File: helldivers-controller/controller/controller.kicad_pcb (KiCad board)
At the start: 4 copper layers, 71 x 57 mm, 9 parts, among them SW10 SW_Push, SW11 SW_Push, SW2 SW_SPDT, SW3 SW_SPDT, SW4 SW_SPDT, SW5 SW_SPDT, SW8 SW_Push, SW9 SW_Push, U1 Sparkfun_Pro_Micro

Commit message: added graphics and gerber files
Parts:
- added G***: LOGO, LOGO, F.Cu at (163.0, 70.6)
- added REF**: MountingHole_2.2mm_M2, MountingHole:MountingHole_2.2mm_M2, F.Cu at (178.0, 112.0)
- added REF**: MountingHole_2.2mm_M2, MountingHole:MountingHole_2.2mm_M2, F.Cu at (109.0, 56.0)
- added REF**: MountingHole_2.2mm_M2, MountingHole:MountingHole_2.2mm_M2, F.Cu at (177.0, 56.0)
- added REF**: MountingHole_2.2mm_M2, MountingHole:MountingHole_2.2mm_M2, F.Cu at (109.0, 112.0)
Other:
- board size 71 x 57 mm -> 75 x 62.1 mm
- board text added: "JLCJLCJLCJLC"

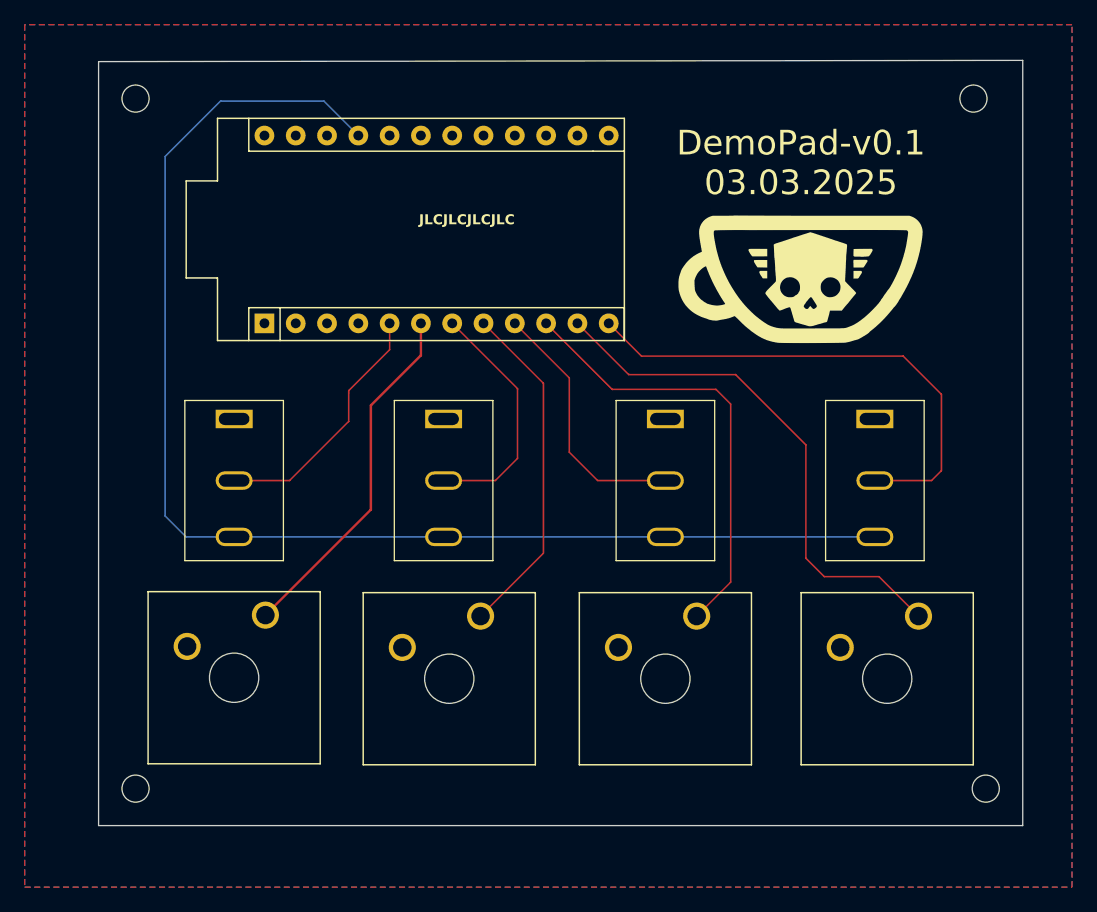
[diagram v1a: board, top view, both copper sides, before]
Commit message: updated code to reflect board diagram
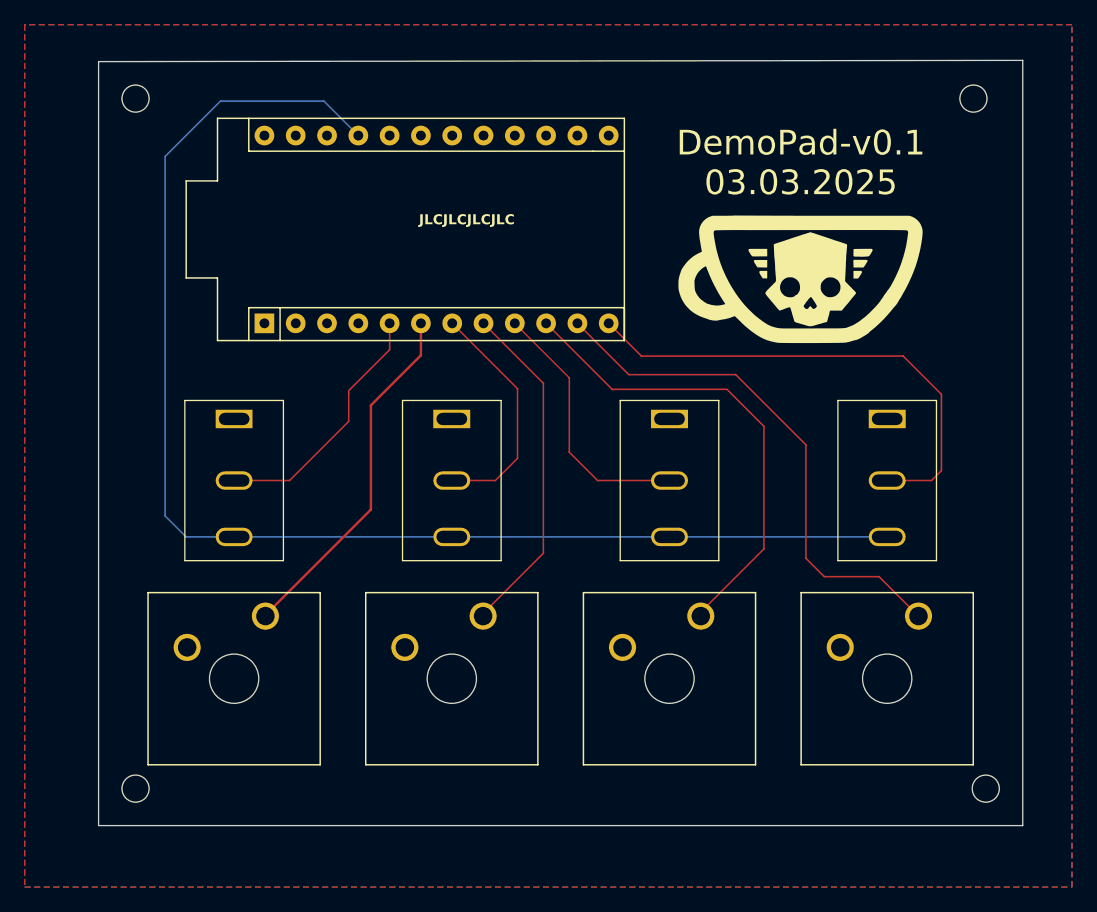
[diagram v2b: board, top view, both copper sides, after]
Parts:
- moved SW5 1.00 mm to (170.0, 87.0)
- moved SW3 0.67 mm to (134.7, 87.0)
- moved SW2 0.33 mm to (152.3, 87.0)
- moved SW8 0.33 mm to (154.9, 98.0)
- moved SW10 0.21 mm to (137.2, 98.0)
- moved SW11 0.08 mm to (119.5, 98.0)
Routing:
- net Net-(U1-D7): track 36.0 -> 38.8 mm
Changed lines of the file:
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@@
 	(footprint "Button_Switch_Keyboard:SW_Cherry_MX_1.50u_Plate"
 		(layer "F.Cu")
-		(at 119.54 97.92)
+		(at 119.54 98)
 		(descr "Cherry MX keyswitch, 1.50u, plate mount, http://cherryamericas.com/wp-content/uploads/2014/12/mx_cat.pdf")
 		(tags "Cherry MX keyswitch 1.50u plate")
@@
 	(footprint "Button_Switch_Keyboard:SW_Cherry_MX_1.50u_Plate"
 		(layer "F.Cu")
-		(at 154.54 98)
+		(at 154.873333 98)
 		(descr "Cherry MX keyswitch, 1.50u, plate mount, http://cherryamericas.com/wp-content/uploads/2014/12/mx_cat.pdf")
 		(tags "Cherry MX keyswitch 1.50u plate")
@@
 	(footprint "AEDIKO-Micro-Toggle-Switch-3-Pin-SPDT-on-on:spdt-on-on-micro-toggle-switch"
 		(layer "F.Cu")
-		(at 152 87 -90)
+		(at 152.333333 87 -90)
 		(property "Reference" "SW2"
 			(at 0 -0.5 270)
@@
 			(polygon
 				(pts
-					(xy 156 80.5) (xy 156 93.5) (xy 148 93.5) (xy 148 80.5)
+					(xy 156.333333 80.5) (xy 156.333333 93.5) (xy 148.333333 93.5) (xy 148.333333 80.5)
 				)
 			)
@@
 	(footprint "AEDIKO-Micro-Toggle-Switch-3-Pin-SPDT-on-on:spdt-on-on-micro-toggle-switch"
 		(layer "F.Cu")
-		(at 134 87 -90)
+		(at 134.666667 87 -90)
 		(property "Reference" "SW3"
 			(at 0 -0.5 270)
@@
 			(polygon
 				(pts
-					(xy 138 80.5) (xy 138 93.5) (xy 130 93.5) (xy 130 80.5)
+					(xy 138.666667 80.5) (xy 138.666667 93.5) (xy 130.666667 93.5) (xy 130.666667 80.5)
 				)
 			)
@@
 	(footprint "Button_Switch_Keyboard:SW_Cherry_MX_1.50u_Plate"
 		(layer "F.Cu")
-		(at 137 98)
+		(at 137.206667 98)
 		(descr "Cherry MX keyswitch, 1.50u, plate mount, http://cherryamericas.com/wp-content/uploads/2014/12/mx_cat.pdf")
 		(tags "Cherry MX keyswitch 1.50u plate")
@@
 	(footprint "AEDIKO-Micro-Toggle-Switch-3-Pin-SPDT-on-on:spdt-on-on-micro-toggle-switch"
 		(layer "F.Cu")
-		(at 169 87 -90)
+		(at 170 87 -90)
 		(property "Reference" "SW5"
 			(at 0 -0.5 270)
@@
 			(polygon
 				(pts
-					(xy 173 80.5) (xy 173 93.5) (xy 165 93.5) (xy 165 80.5)
+					(xy 174 80.5) (xy 174 93.5) (xy 166 93.5) (xy 166 80.5)
 				)
 			)
@@
 	)
 	(segment
-		(start 157.3 80.8)
-		(end 157.3 95.24)
+		(start 160 92.54)
+		(end 154.54 98)
 		(width 0.127)
 		(layer "F.Cu")
@@
 	)
 	(segment
-		(start 156.1 79.6)
-		(end 157.3 80.8)
+		(start 160 82.594537)
+		(end 160 92.54)
 		(width 0.127)
 		(layer "F.Cu")
@@
 	)
 	(segment
-		(start 157.3 95.24)
-		(end 154.54 98)
+		(start 147.68 79.6)
+		(end 157.005463 79.6)
 		(width 0.127)
 		(layer "F.Cu")
@@
 	)
 	(segment
-		(start 147.68 79.6)
-		(end 156.1 79.6)
+		(start 157.005463 79.6)
+		(end 160 82.594537)
 		(width 0.127)
 		(layer "F.Cu")
@@
 		(min_thickness 0.25)
 		(filled_areas_thickness no)
-		(fill yes
+		(fill
 			(thermal_gap 0.5)
 			(thermal_bridge_width 0.5)
